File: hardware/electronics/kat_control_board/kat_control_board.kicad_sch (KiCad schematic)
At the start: 122 parts, among them J1 USB_C_Receptacle_USB2.0, J10 Conn_01x04, J11 Conn_01x04, J12 Conn_01x04, J13 Conn_01x04, J14 Conn_01x04, J15 Conn_01x04, J16 Conn_01x04, J17 Conn_01x02, J18 Conn_01x04, J19 Conn_01x04, J2 Conn_01x04, J20 Conn_01x02, J21 Conn_01x02, J22 Conn_01x02, J23 Conn_01x02, J24 Conn_01x02, J25 Conn_01x02, J26 Conn_01x02, J27 Conn_01x02, J28 Conn_01x04, J29 Conn_02x30_Odd_Even, J3 Conn_01x04, J30 Conn_02x30_Odd_Even, J31 Conn_02x30_Odd_Even, J32 Conn_02x30_Odd_Even, J4 Conn_01x04, J5 Conn_01x04, J6 Conn_01x04, J7 Conn_01x04, J8 Conn_01x04, J9 Conn_01x04, Q1 AO3400A, Q2 AO3400A, Q3 AO3400A, Q4 AO3400A, Q5 AO3400A, SW1 SW_SPST, SW2 SW_SPST, U1 RP2040, U2 W25Q128JVS, U3 SN74HC4851, U4 74HCT244, U5 74HCT244, U6 SIC431, U7 XC6206PxxxMR, Y1 12MHz

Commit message: Updated PCB design with more protections
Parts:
- removed U4, U5: 74HCT244, Package_SO:TSSOP-20_4.4x6.5mm_P0.65mm, symbol 74xx:74HCT244
- added D5: M7, Diode_SMD:D_SMA, symbol Device:D
- added D6: RED, LED_SMD:LED_0603_1608Metric, symbol Device:LED
- added D7: YELLOW, LED_SMD:LED_0603_1608Metric, symbol Device:LED
- added H4: MountingHole, MountingHole:MountingHole_3.5mm_Pad_Via, symbol Mechanical:MountingHole
- added J33: Conn_01x03, Connector_PinHeader_2.54mm:PinHeader_1x03_P2.54mm_Vertical, symbol Connector_Generic:Conn_01x03
- added R42, R43, R44, R45, R46, R47, R48, R49, R50: 100R, Resistor_SMD:R_0402_1005Metric, symbol Device:R
- added R51, R53: 1kR, Resistor_SMD:R_0402_1005Metric, symbol Device:R
- added R52: 7.5kR, Resistor_SMD:R_0402_1005Metric, symbol Device:R
- added R54: 330R, Resistor_SMD:R_0402_1005Metric, symbol Device:R
- added U10, U11, U12, U13, U5, U9: SRV05-4, Package_TO_SOT_SMD:SOT-23-6, symbol Power_Protection:SRV05-4
- added U4, U8: 74HCT541, Package_SO:TSSOP-20_4.4x6.5mm_P0.65mm, symbol 74xx:74HCT541
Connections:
- net +12V: now also D5.1 (K), R52.1, R53.2
- net +3V3: now also U5.5 (VP), U9.5 (VP)
- net +5V: now also U10.5 (VP), U11.5 (VP), U12.5 (VP), U13.5 (VP), U4.20 (VCC), U8.20 (VCC)
- net GND: now also D5.2 (A), D6.1 (K), D7.1 (K), J33.2 (Pin_2), R51.2, U10.2 (VN), U11.2 (VN), U12.2 (VN), U13.2 (VN), U4.10 (GND), U5.2 (VN), U8.10 (GND), U9.2 (VN)
- net LED0: now also U10.1 (IO1)
- net LED1: now also U10.3 (IO2)
- net LED10: now also U11.4 (IO3)
- net LED11: now also U11.6 (IO4)
- net LED12: now also U13.1 (IO1)
- net LED13: now also U13.3 (IO2)
- net LED14: now also U13.4 (IO3)
- net LED15: now also U13.6 (IO4)
- net LED2: now also U10.4 (IO3)
- net LED3: now also U10.6 (IO4)
- net LED4: now also U12.1 (IO1)
- net LED5: now also U12.3 (IO2)
- net LED6: now also U12.4 (IO3)
- net LED7: now also U12.6 (IO4)
- net LED8: now also U11.1 (IO1)
- net LED9: now also U11.3 (IO2)
- net PULL0: now also R49.1; no longer J17.1 (Pin_1)
- net PULL1: now also R48.1; no longer J20.1 (Pin_1)
- net PULL2: now also R50.1; no longer J21.1 (Pin_1)
- net PULL3: now also R47.1; no longer J22.1 (Pin_1)
- net PULL4: now also R46.1; no longer J23.1 (Pin_1)
- net SW0: now also U1.28 (GPIO17), R42.1; no longer Q2.1 (G), R38.1, U1.27 (GPIO16)
- net SW1: now also U1.29 (GPIO18), R43.1; no longer Q4.1 (G), R40.1, U1.28 (GPIO17)
- net SW2: now also U1.30 (GPIO19), R44.1; no longer Q3.1 (G), R39.1, U1.29 (GPIO18)
- net SW3: now also U1.31 (GPIO20), R45.1; no longer Q5.1 (G), R41.1, U1.30 (GPIO19)
- net USB_DM: now also U5.3 (IO2)
- net USB_DP: now also U5.1 (IO1)
- net ~{LED_PWR}: now also U4.1 (G1), U4.19 (G2), U8.1 (G1), U8.19 (G2)
- net at R11.1: now also U8.16 (Y2)
- net at R21.1: now also U4.15 (Y3)
- net at R15.1: now also U4.13 (Y5)
- net LED8_IN: now reaches U1.11 (GPIO8)
- net LED8_IN: now also U4.9 (A7)
- net LED9_IN: now reaches U1.12 (GPIO9)
- net LED9_IN: now also U4.8 (A6)
- net LED10_IN: now reaches U1.13 (GPIO10)
- net LED10_IN: now also U4.7 (A5)
- net LED11_IN: now reaches U1.14 (GPIO11)
- net LED11_IN: now also U4.6 (A4)
- net LED12_IN: now reaches U1.15 (GPIO12)
- net LED12_IN: now also U4.5 (A3)
- net LED13_IN: now reaches U1.16 (GPIO13)
- net LED13_IN: now also U4.4 (A2)
- net LED14_IN: now reaches U1.17 (GPIO14)
- net LED14_IN: now also U4.3 (A1)
- net LED15_IN: now reaches U1.18 (GPIO15)
- net LED15_IN: now also U4.2 (A0)
- net LED0_IN: now reaches U1.2 (GPIO0)
- net LED0_IN: now also U8.9 (A7)
- net at U1.24 (SWCLK): now also J33.1 (Pin_1)
- net at U1.25 (SWD): now also J33.3 (Pin_3)
- net LED1_IN: now reaches U1.3 (GPIO1)
- net LED1_IN: now also U8.8 (A6)
- net LED2_IN: now reaches U1.4 (GPIO2)
- net LED2_IN: now also U8.7 (A5)
- net LED3_IN: now reaches U1.5 (GPIO3)
- net LED3_IN: now also U8.6 (A4)
- net LED4_IN: now reaches U1.6 (GPIO4)
- net LED4_IN: now also U8.5 (A3)
- net LED5_IN: now reaches U1.7 (GPIO5)
- net LED5_IN: now also U8.4 (A2)
- net LED6_IN: now reaches U1.8 (GPIO6)
- net LED6_IN: now also U8.3 (A1)
- net LED7_IN: now reaches U1.9 (GPIO7)
- net LED7_IN: now also U8.2 (A0)
- net at R9.1: now also U8.14 (Y4)
- net at R8.1: now also U8.13 (Y5)
- net at R7.1: now also U8.12 (Y6)
- net at R6.1: now also U8.11 (Y7)
- net at R10.1: now also U8.15 (Y3)
- net at R12.1: now also U8.17 (Y1)
- net at R13.1: now also U8.18 (Y0)
- net at R17.1: now also U4.11 (Y7)
- net at R16.1: now also U4.12 (Y6)
- net at R14.1: now also U4.14 (Y4)
- net at R18.1: now also U4.18 (Y0)
- net at R19.1: now also U4.17 (Y1)
- net at R20.1: now also U4.16 (Y2)
- net 12V_SENSE: now reaches U3.1 (X4)
- net 12V_SENSE: now also R51.1, R52.2
- net A0: now reaches U3.2 (X6)
- net A0: now also J29.3 (Pin_3)
- net A1: now reaches U3.4 (X7)
- net A1: now also J29.4 (Pin_4)
- new net: D7.2 (A), R54.1
- new net: Q5.1 (G), R41.1, R45.2
- new net: J17.1 (Pin_1), R49.2
- new net: J20.1 (Pin_1), R48.2
- new net: J22.1 (Pin_1), R47.2
- new net: Q3.1 (G), R39.1, R44.2
- new net: Q2.1 (G), R38.1, R42.2
- new net: J21.1 (Pin_1), R50.2
- new net: Q4.1 (G), R40.1, R43.2
- new net: J23.1 (Pin_1), R46.2
- new net: D6.2 (A), R53.1
- new net STATUS_LED: R54.2, U1.27 (GPIO16)
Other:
- note added: "Crowbar"
- moved on the sheet: C1, C10, C11, C12, C13, C14, C15, C16, C17, C18, C19, C2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

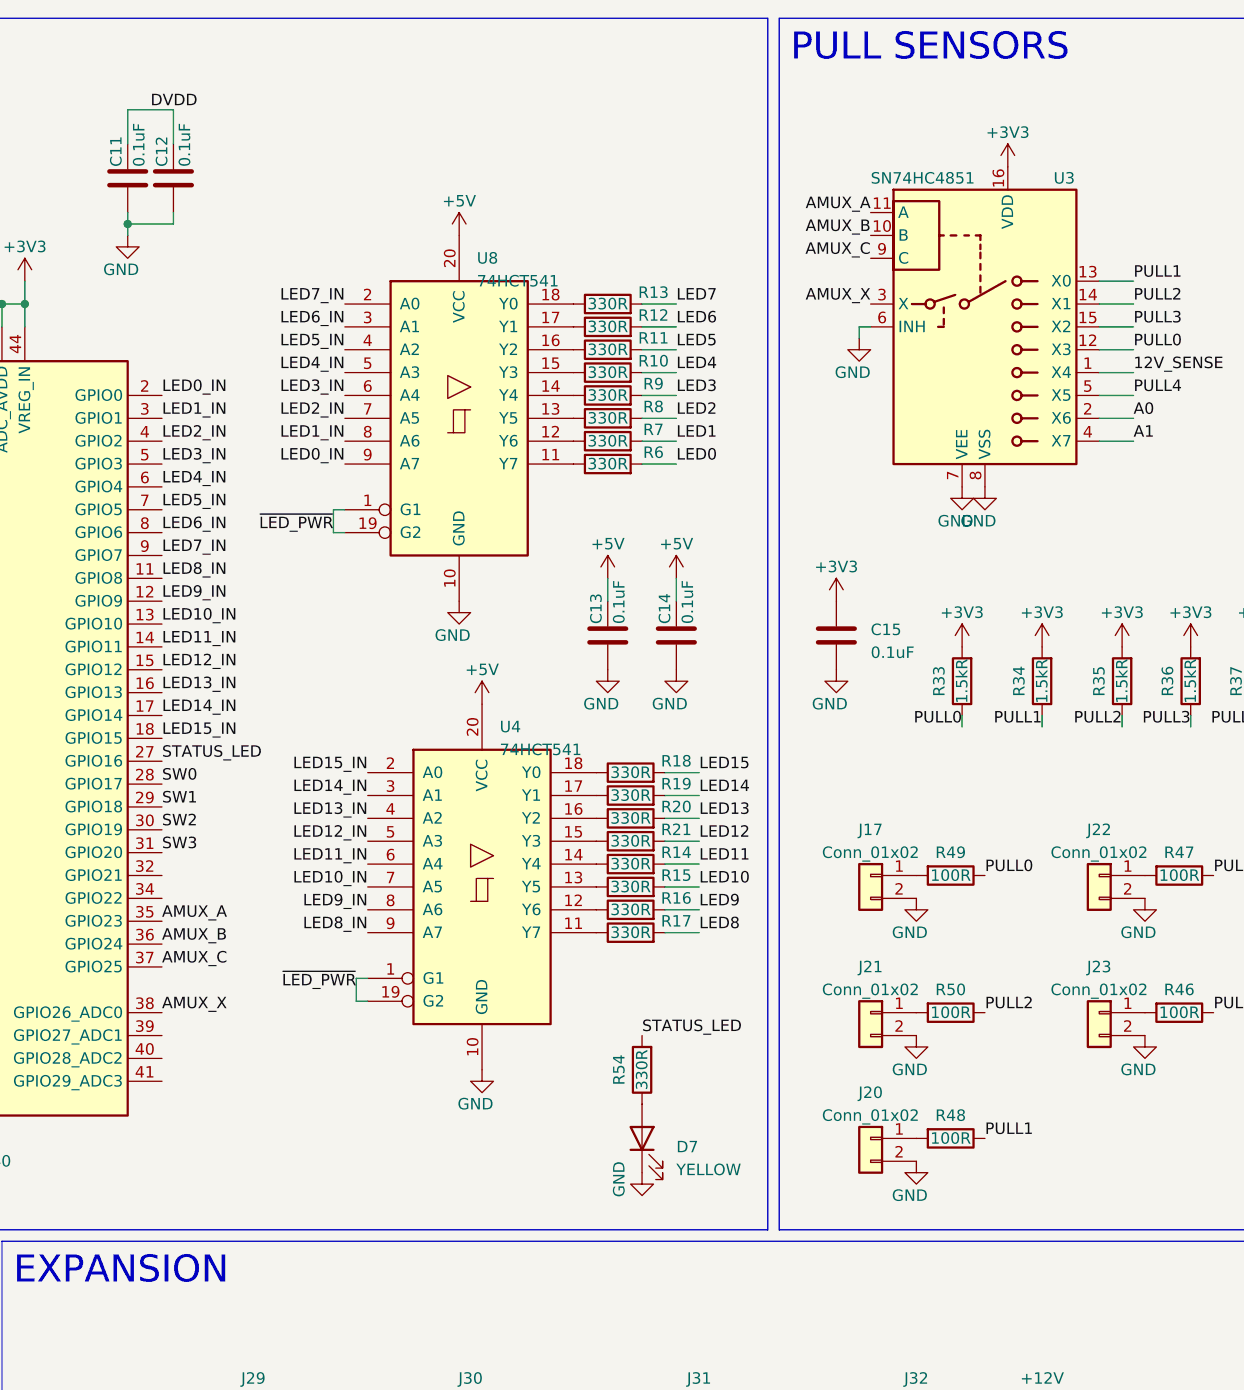
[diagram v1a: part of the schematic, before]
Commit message: Added test firmware
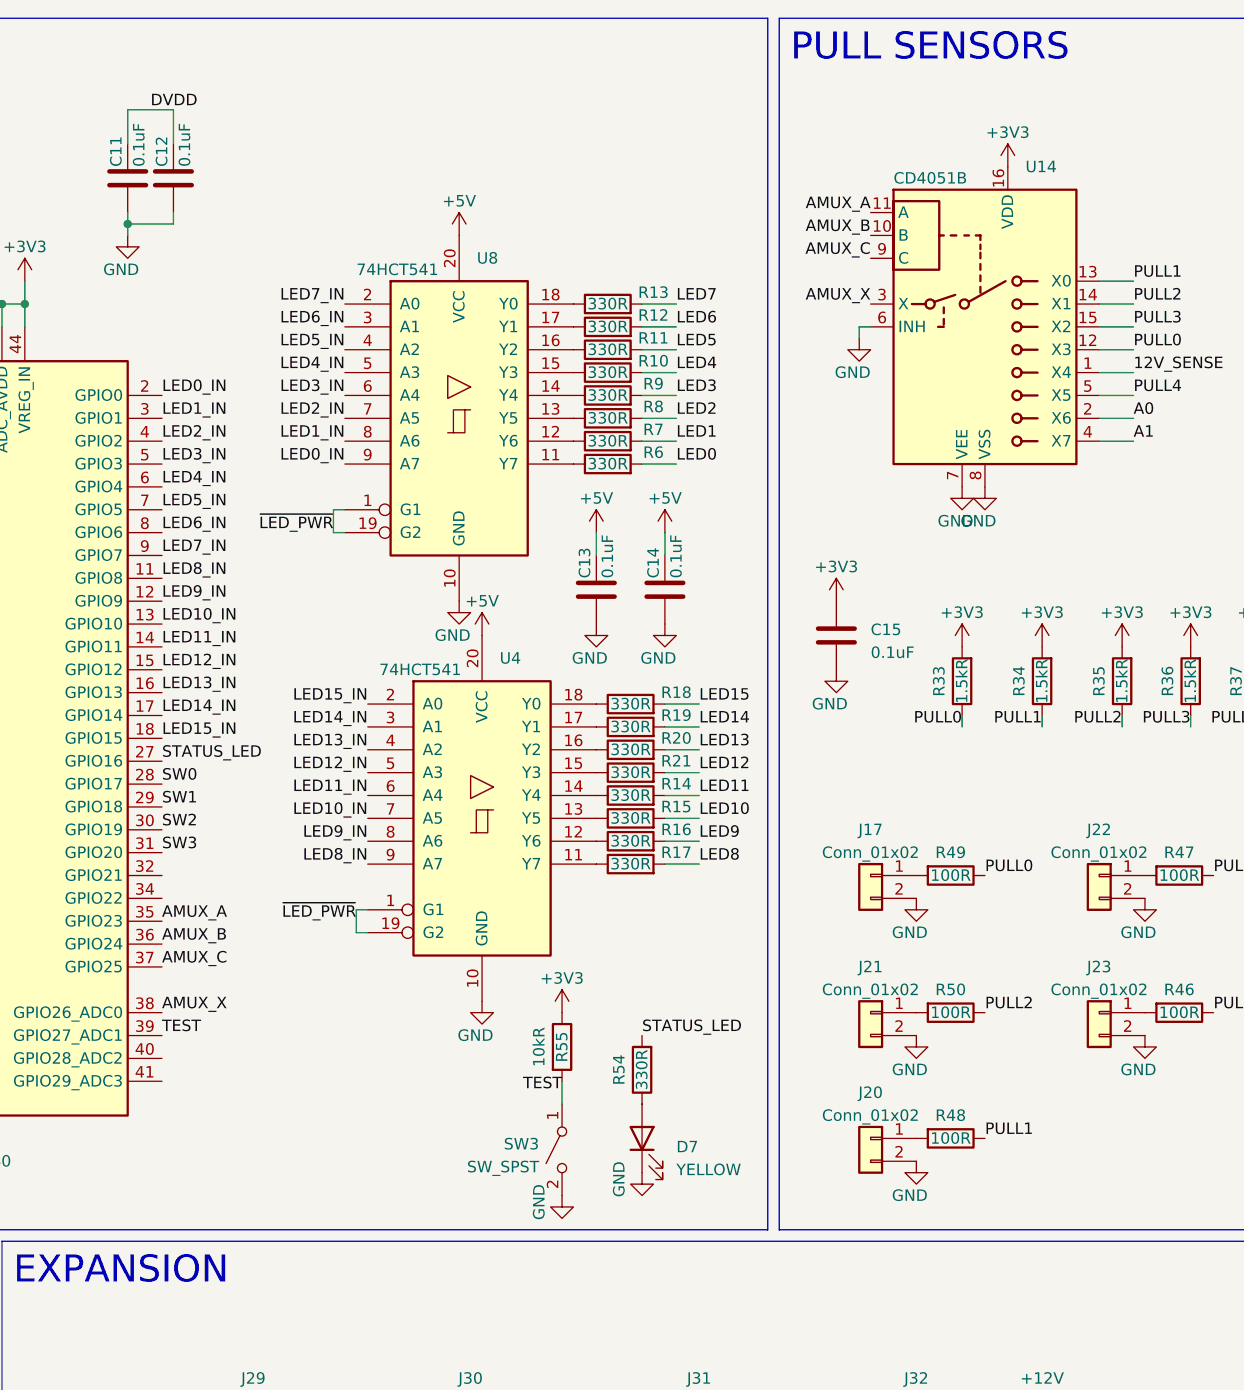
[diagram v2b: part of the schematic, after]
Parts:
- removed U3: SN74HC4851, Package_SO:TSSOP-16_4.4x5mm_P0.65mm, symbol Analog_Switch:CD4051B
- added R55: 10kR, Resistor_SMD:R_0402_1005Metric, symbol Device:R
- added SW3: SW_SPST, M_SW:TS-1187A-B-A-B, symbol Switch:SW_SPST
- added U14: CD4051B, Package_SO:SOIC-16_3.9x9.9mm_P1.27mm, symbol Analog_Switch:CD4051B
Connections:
- net +3V3: now also R55.1, U14.16 (VDD)
- net 12V_SENSE: now also U14.1 (X4)
- net A0: now also U14.2 (X6)
- net A1: now also U14.4 (X7)
- net AMUX_A: now also U14.11 (A)
- net AMUX_B: now also U14.10 (B)
- net AMUX_C: now also U14.9 (C)
- net AMUX_X: now also U14.3 (X)
- net GND: now also SW3.2 (B), U14.6 (INH), U14.7 (VEE), U14.8 (VSS)
- net PULL0: now also U14.12 (X3)
- net PULL1: now also U14.13 (X0)
- net PULL2: now also U14.14 (X1)
- net PULL3: now also U14.15 (X2)
- net PULL4: now also U14.5 (X5)
- net TEST: now reaches U1.39 (GPIO27_ADC1)
- net TEST: now also R55.2, SW3.1 (A)
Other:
- moved on the sheet: C13, C14, R14, R15, R16, R17, R18, R19, R20, R21, U4

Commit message: Fixed PGOOD pull up part number
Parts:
- R22: JLC C25086 -> C25741
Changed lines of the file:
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@@
       (effects (font (size 1.27 1.27)) hide)
     )
-    (property "JLC" "C25086" (at 53.34 219.71 90)
+    (property "JLC" "C25741" (at 53.34 219.71 90)
       (effects (font (size 1.27 1.27)) hide)
     )

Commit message: Controller board WIP
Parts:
- R30, R32: JLC C25086 -> C11702
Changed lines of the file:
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@@
       (effects (font (size 1.27 1.27)) hide)
     )
-    (property "JLC" "C25086" (at 50.8 116.84 90)
+    (property "JLC" "C11702" (at 50.8 116.84 90)
       (effects (font (size 1.27 1.27)) hide)
     )
@@
       (effects (font (size 1.27 1.27)) hide)
     )
-    (property "JLC" "C25086" (at 104.14 59.69 90)
-      (effects (font (size 1.27 1.27)) hide)
-    )
+    (property "JLC" "C11702" (at 104.14 59.69 90)
+      (effects (font (size 1.27 1.27)) hide)
+    )
+    (property "Field5" "" (at 104.14 59.69 90)
+      (effects (font (size 1.27 1.27)) hide)
+    )
